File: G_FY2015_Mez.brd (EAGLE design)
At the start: 160 x 100 mm, 182 parts, among them IC100 FT232RL, J1 RPI2_GPIO_HOLES, J100 EPL.00.250.NTN, J101 EPL.00.250.NTN, J102 EPL.00.250.NTN, J103 EPL.00.250.NTN, J180 TOKUDEN_SP6, J181 USB Mini-B Connector, J2 SPACEWIRE_MDMMDM9, J300 SHV_PIGTAIL_LAND, J301 SHV_PIGTAIL_LAND, J600_12V IL-4P-S3EN2, J610 2.1MMJACKTHM, U10 LM60, U100 AD9215, U101 AD8138, U102 LM6142, U11 MCP4822-E/SN, U110 AD9215, U111 AD8138, U112 LM6142, U120 AD9215, U121 AD8138, U122 LM6142, U130 AD9215, U131 AD8138, U132 LM6142, U190 SN65LVDS049, U191 GPS_FGPMMOPA6H, U192 LED-5, U300 OPTON_1PA_12, U301 OPTON_1PA_12, U302 2SC1815, U303 2SJ313, U5 MCP3208-CI/SL, U500 LT6106, U510 LT6106, U6 MCP1525TSOT-23-3, U600 PHT12050WAH, U610 PHT12050WAH, U620 LTC1983ES6-3, U7 LM60, U8 LM60, U9 LM60

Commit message: version 20150904 (placement completed; before replacing with complementray SMD resistor and cap)
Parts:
- removed C192: 100n, Aardvark:3216
- removed C193: 4.7u, Aardvark:3216
- removed J102, J103: EPL.00.250.NTN, Aardvark:EPL.00.250.NTN
- removed JP1: (no value), pinhead:2X02
- removed JP100, TP_SPI: (no value), pinhead:1X05
- removed JP101: (no value), pinhead:1X06
- removed P_IN0, P_IN1, P_IN2, P_IN3, TP5: TPPAD1-13, Aardvark:P1-13
- removed R195, R196: 100, Aardvark:2012
- removed SJ1: (no value), Aardvark:SJ_2W
- removed U$27: (no value), Aardvark:AARDVARK_LOGO
- removed U$28: (no value), Aardvark:GROWTH_FY2015_LOGO
- removed U10, U9: LM60, Aardvark:TO-92-R2.5C
- removed U11: MCP4822-E/SN, Aardvark:SOIC-8(150MIL)(1.27MM)
- removed U190: SN65LVDS049, Aardvark:SO-16LD
- added C18: 1u, Aardvark:3216
- added C20, C22, C24, C26: 10u, Aardvark:3216
- added C21, C23, C25: 0.1u, Aardvark:3216
- added J110, J120, J130: EPL.00.250.NTN, Aardvark:EPL.00.250.NTN
- added J111, J121, J131, J620: IL-2P-S3EN2, Aardvark:IL-2P-S3EN2
- added J3: IL-3P-S3EN2, Aardvark:IL-3P-S3EN2
- added J4_I2C, J650_VOUT: IL-4P-S3EN2, Aardvark:IL-4P-S3EN2
- added J630, J640: USB_TYPEA_LUMBERG_2410_01, Aardvark:LUMBERG_2410-01
- added JP101_TRIG_OUT: (no value), Aardvark:2X07
- added JP_LCD: LCD16X2, Aardvark:LCD16X2
- added JP_SPI: (no value), Aardvark:1X05
- added R109, R119, R129, R139: 50, Aardvark:2012
- added R192: 2k, Aardvark:2012
- added R193: 1k, Aardvark:2012
- added SJ100, SJ110, SJ120, SJ130, SJ_ADC_MODE: (no value), Aardvark:SJ_2W
- added VR_CONT: (no value), Aardvark:ADJRP3-9.70XW5.0X9.80MM
- C19: value 100n -> 0.1u
- J101: value EPL.00.250.NTN -> IL-2P-S3EN2; device Aardvark:EPL.00.250.NTN -> Aardvark:IL-2P-S3EN2
- J2: value SPACEWIRE_MDMMDM9 -> IL-3P-S3EN2; device Aardvark:MDM_9_PCB -> Aardvark:IL-3P-S3EN2
- R190: value 1k -> 3k
- R500, R510: value 0.1 -> 0.01
- U100, U110, U120, U130: value AD9215 -> AD9215LONG_PAD; device Aardvark:TSSOP-28(4.4MM)(0.65MM) -> Aardvark:TSSOP-28(4.4MM)(0.65MM)_LONGPAD
- VR100, VR110, VR120, VR130: value 1k -> (none)
- moved U7 110.8 mm to (25.6, 27.9)
- moved TP_GND2 106.2 mm to (94.0, 2.17), turned to 90 degrees
- moved U510 71.7 mm to (91.9, 15.0)
- moved R510 70.5 mm to (91.2, 22.1), turned to 270 degrees
- moved R511 69.2 mm to (84.0, 19.7)
- moved R199 64.2 mm to (136.7, 24.6), flipped to the bottom, turned to 90 degrees
- moved R117 59.7 mm to (129.7, 42.8), turned to 0 degrees
- moved R115 57.6 mm to (134.7, 34.0), turned to 0 degrees
- moved R110 57.6 mm to (129.6, 37.9)
- moved R111 57.6 mm to (134.6, 37.9)
- moved R512 57.0 mm to (84.0, 24.7)
- moved R132 56.8 mm to (41.5, 9.35), flipped to the bottom, turned to 180 degrees
- moved P_OUT3 56.6 mm to (49.6, 26.1)
- moved TP_GND 56.5 mm to (5.70, 83.9)
- moved R137 55.9 mm to (45.4, 26.9), turned to 90 degrees
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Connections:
- removed net SLOWDAC_/LDAC: J1.P$3, U11.5
- removed net SLOWDAC_0: JP1.1, U11.8
- removed net SLOWDAC_1: JP1.3, U11.6
- removed net SPW_DIN_N: J2.6, R195.2, U190.1
- removed net SPW_DIN_P: J2.1, R195.1, U190.2
- removed net SPW_DOUT_N: J2.5, U190.8
- removed net SPW_DOUT_P: J2.9, U190.7
- removed net SPW_SIN_N: J2.7, R196.2, U190.4
- removed net SPW_SIN_P: J2.2, R196.1, U190.3
- removed net SPW_SOUT_N: J2.4, U190.5
- removed net SPW_SOUT_P: J2.8, U190.6
- removed net VREF_3V3_1/2: R190.2, R191.1, SJ1.1
- new net LCD_D4: J1.P$31, JP_LCD.11
- new net LCD_D5: J1.P$33, JP_LCD.12
- new net LCD_D6: J1.P$35, JP_LCD.13
- new net LCD_D7: J1.P$37, JP_LCD.14
- new net LCD_ENA: J1.P$40, JP_LCD.6
- new net LCD_RS: J1.P$38, JP_LCD.4
- new net LCD_V_CONT: JP_LCD.3, VR_CONT.2
- new net N$100: P_OUT0.TP, R109.2, U102.7, VR100.2
- new net N$101: R109.1, SJ100.1
- new net N$102: R119.1, SJ110.1
- new net N$103: R129.1, SJ120.1
- new net N$104: R139.1, SJ130.1
- new net N$34: J630.D-
- new net N$88: J630.D+
- new net N$89: J640.D-
- new net N$90: J640.D+
- new net N$91: JP101_TRIG_OUT.11
- new net N$92: P_OUT1.TP, R119.2, U112.7, VR110.2
- new net N$93: P_OUT2.TP, R129.2, U122.7, VR120.2
- new net N$94: JP_LCD.8
- new net N$95: JP_LCD.9
- new net N$96: JP_LCD.10
- new net N$97: JP_LCD.7
- new net N$98: P_OUT3.TP, R139.2, U132.7, VR130.2
- new net N$99: R192.2, R193.1, SJ_ADC_MODE.3
- new net RPI_I2C_SCL: J1.P$5, J4_I2C.P$2
- new net RPI_I2C_SDA: J1.P$3, J4_I2C.P$3
- net +3V3: now also C18.2, C20.2, C21.2, C22.2, C23.2, C24.2, C25.2, C26.2, J2.P$1, J3.P$1, J4_I2C.P$1, J650_VOUT.P$2, JP101_TRIG_OUT.14, R192.1; no longer C190.1, C191.1, C192.2, C193.2, IC100.20, IC100.4, U10.1, U11.1, U190.12, U190.16, U9.1
- net +5V: now also C190.1, C191.1, IC100.20, IC100.4, J620.P$1, J630.VBUS, J640.VBUS, J650_VOUT.P$1, JP101_TRIG_OUT.2, JP_LCD.1, VR_CONT.1; no longer J180.81
- net -3V3: now also J650_VOUT.P$3
- net ADC_CM: now also R190.2, R191.1; no longer SJ1.2
- net ADC_MODE: now also SJ_ADC_MODE.2; no longer J180.24
- net AGND: now also VR100.3, VR110.3, VR120.3, VR130.3; no longer VR100.1, VR110.1, VR120.1, VR130.1
- net FPGA_GPIO0: now also JP101_TRIG_OUT.9; no longer JP101.5
- net GND: now also C18.1, C20.1, C21.1, C22.1, C23.1, C24.1, C25.1, C26.1, J110.S1, J120.S1, J130.S1, J2.P$3, J3.P$3, J4_I2C.P$4, J620.P$2, J630.GND, J630.GND1, J630.GND2, J640.GND, J640.GND1, J640.GND2, J650_VOUT.P$4, JP101_TRIG_OUT.13, JP_LCD.2, JP_LCD.5, R193.2, SJ_ADC_MODE.1, VR300.3, VR301.3, VR_CONT.3; no longer C192.1, C193.1, J101.S1, J102.S1, J103.S1, J180.82, J2.3, J2.THREAD_1, J2.THREAD_2, JP1.2, JP1.4, JP101.6, U10.3, U11.7, U190.13, U190.9, U9.3, VR300.1, VR301.1
- net N$21: no longer JP100.1
- net N$22: no longer JP100.2
- net N$29: no longer JP100.3
- net N$30: no longer JP100.4
- net N$31: no longer JP100.5
- net N$35: no longer TP5.TP
- net N$5: now also VR300.1; no longer VR300.3
- net N$58: no longer P_IN0.TP
- net N$62: now also VR100.1; no longer VR100.2
- net N$7: now also VR301.1; no longer VR301.3
- net N$70: now also J110.1; no longer J101.1, P_IN1.TP
- net N$72: now also VR110.1; no longer VR110.2
- net N$75: now also J120.1; no longer J102.1, P_IN2.TP
- net N$77: now also VR120.1; no longer VR120.2
- net N$80: now also J130.1; no longer J103.1, P_IN3.TP
- net N$82: now also VR130.1; no longer VR130.2
- net PREAMP0_OUT: now also SJ100.2; no longer P_OUT0.TP, U102.7, VR100.3
- net PREAMP1_OUT: now also SJ110.2; no longer P_OUT1.TP, U112.7, VR110.3
- net PREAMP2_OUT: now also SJ120.2; no longer P_OUT2.TP, U122.7, VR120.3
- net PREAMP3_OUT: now also SJ130.2; no longer P_OUT3.TP, U132.7, VR130.3
- net SLOWADC_0: no longer SJ1.3
- net SLOWADC_2: now also J3.P$2; no longer U9.2
- net SLOWADC_3: now also J2.P$2; no longer U10.2
- net SPI_CE0: now also JP_SPI.4; no longer TP_SPI.4
- net SPI_CE1: now also JP_SPI.5; no longer TP_SPI.5, U11.2
- net SPI_MISO: now also JP_SPI.2; no longer TP_SPI.2
- net SPI_MOSI: now also JP_SPI.3; no longer TP_SPI.3, U11.4
- net SPI_SCLK: now also JP_SPI.1; no longer TP_SPI.1, U11.3
- net SPW_DIN: no longer U190.15
- net SPW_DOUT: no longer U190.10
- net SPW_SIN: no longer U190.14
- net SPW_SOUT: no longer U190.11
- net TRIG_OUT0: now also JP101_TRIG_OUT.1; no longer JP101.1
- net TRIG_OUT1: now also JP101_TRIG_OUT.3; no longer JP101.2
- net TRIG_OUT2: now also JP101_TRIG_OUT.5; no longer JP101.3
- net TRIG_OUT3: now also JP101_TRIG_OUT.7; no longer JP101.4
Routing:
- net GND: track 1382.9 -> 0.00 mm, vias 12 -> 0
- net +3V3: track 600.1 -> 0.00 mm, vias 19 -> 0
- net -3V3: track 285.5 -> 0.00 mm, vias 9 -> 0
- net +5V: track 217.6 -> 0.00 mm, vias 2 -> 0
- net ADC_CM: track 186.8 -> 0.00 mm, vias 2 -> 0
- net GPS_1PPS: track 133.0 -> 0.00 mm, vias 2 -> 0
- net SLOWADC_5: track 125.4 -> 0.00 mm, vias 5 -> 0
- net SLOWADC_4: track 121.8 -> 0.00 mm, vias 3 -> 0
- net ADC_PDWN: track 117.6 -> 0.00 mm, vias 4 -> 0
- net SLOWADC_0: track 116.4 -> 0.00 mm, vias 4 -> 0
- net HV_PWR_ENADIS: track 112.7 -> 0.00 mm, vias 2 -> 0
- net ADC_MODE: track 107.9 -> 0.00 mm, vias 3 -> 0
- net +12V: track 106.1 -> 0.00 mm, vias 1 -> 0
- net TRIG_OUT2: track 105.2 -> 0.00 mm
- net PREAMP0_OUT: track 103.9 -> 0.00 mm, vias 1 -> 0
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- removed copper zone on layer 1, net GND
- removed copper zone on layer 16, net GND
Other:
- board text added: "GROWTH-FY2015 Electronics Board Version 20150904"
- board text removed: "GROWTH-FW2015 Electronics Board Version 20150519"

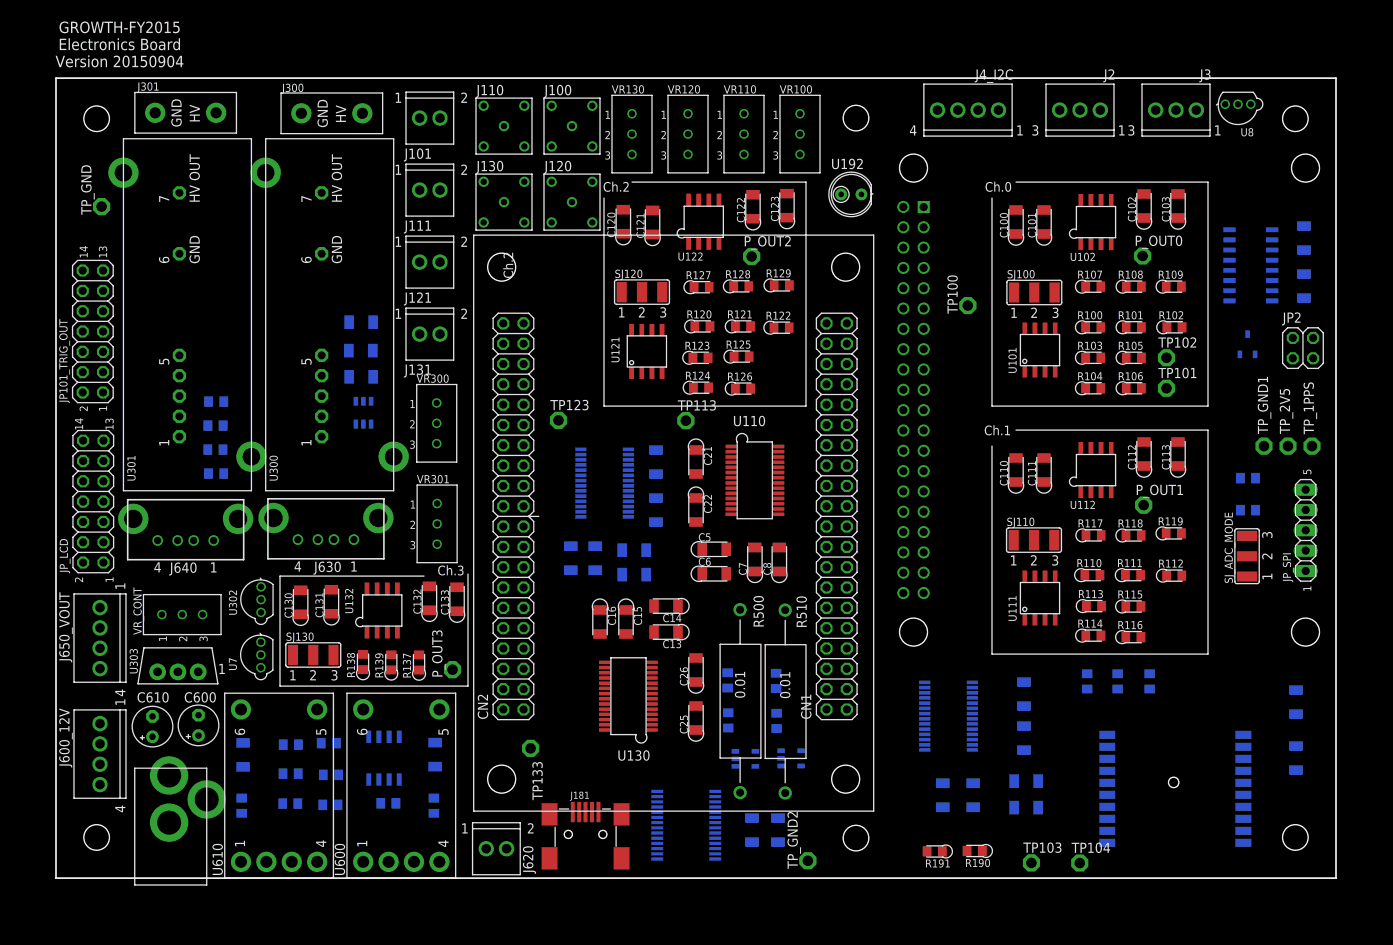
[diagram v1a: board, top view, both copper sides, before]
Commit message: as of 20150911 (4ch, FT232RL) before adding FT245 for higher data transfer rate
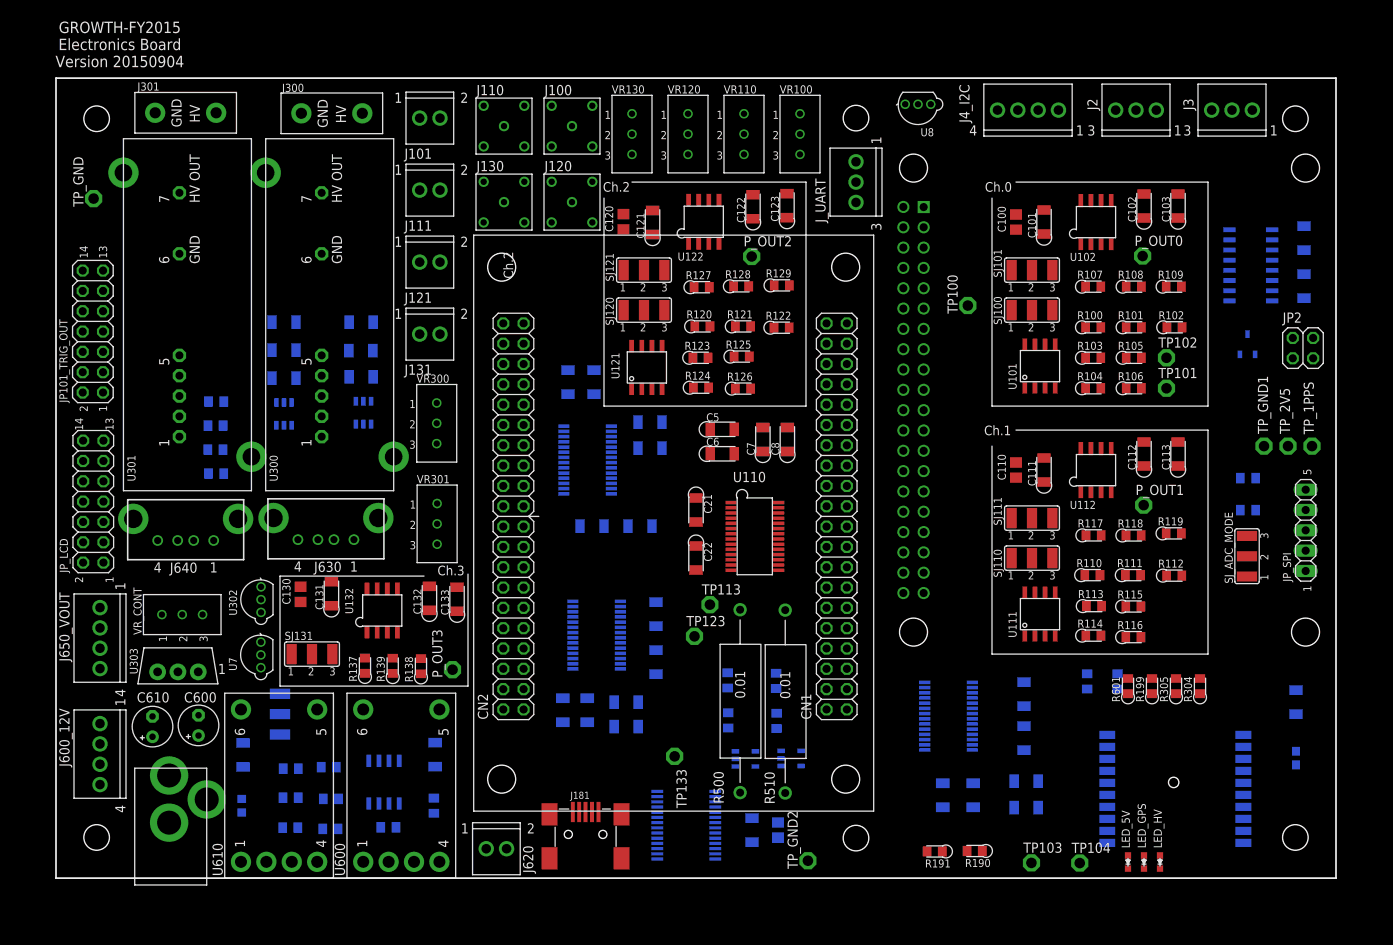
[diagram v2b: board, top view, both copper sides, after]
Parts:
- removed U192: LED-5, Aardvark:LED-5
- added C623, C624: 10u, Aardvark:3216
- added C625: 1u, Aardvark:3216
- added J_UART: IL-3P-S3EN2, Aardvark:IL-3P-S3EN2
- added LED_5V, LED_GPS, LED_HV: LED_1608, Aardvark:LED_1608
- added R304, R305: 1.2k, Aardvark:2012
- added R601: 82, Aardvark:2012
- added SJ101, SJ111, SJ121, SJ131: (no value), Aardvark:SJ_2W
- added U621: LTC1983ES6-5, Aardvark:SOT-23
- C100, C110, C120, C130, C191: device Aardvark:3216 -> Aardvark:C0805
- C190: value 100n -> 0.1u
- C194: device Aardvark:3216 -> Aardvark:C0603
- R100, R105, R106, R110, R115, R116, R120, R125, R126, R130, R135, R136: value 49.9 -> 51
- R101, R103, R104, R111, R113, R114, R121, R123, R124, R131, R133, R134: value 499 -> 510
- R102, R112, R122, R132: value 523 -> 510
- R109, R119, R129, R139: value 50 -> 51
- R199: value 330 -> 82
- R600: value 280 -> 270
- R610: device Aardvark:2012 -> Aardvark:R0603
- U102, U112, U122, U132: value LM6142 -> LM6172
- moved U8 40.0 mm to (107.8, 96.7)
- moved TP123 31.9 mm to (79.8, 30.2)
- moved C15 30.3 mm to (67.2, 62.0), flipped to the bottom
- moved C16 30.3 mm to (64.0, 62.0), flipped to the bottom
- moved U130 30.0 mm to (66.5, 52.3), flipped to the bottom, turned to 270 degrees
- moved C25 25.0 mm to (73.0, 44.0), flipped to the bottom, turned to 180 degrees
- moved TP113 23.2 mm to (81.7, 34.2)
- moved C13 23.1 mm to (74.2, 53.8), flipped to the bottom
- moved C14 23.1 mm to (74.2, 57.0), flipped to the bottom
- moved C26 22.2 mm to (67.0, 44.0), flipped to the bottom, turned to 180 degrees
- moved C9 19.0 mm to (71.3, 22.0)
- moved C10 19.0 mm to (71.3, 18.9)
- moved C11 19.0 mm to (66.4, 21.0)
- moved C12 19.0 mm to (63.4, 21.0)
- moved U120 19.0 mm to (67.6, 30.4)
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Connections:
- new net -5V: C103.2, C113.2, C123.2, C133.2, C624.1, U102.4, U112.4, U122.4, U132.4, U621.2
- new net AIN_0: J100.1, J101.P$1, SJ100.3, SJ101.1
- new net AIN_1: C110.1, R117.2, SJ110.3, SJ111.2, U112.2
- new net AIN_2: J120.1, J121.P$1, SJ120.3, SJ121.1
- new net AIN_3: J130.1, J131.P$1, SJ130.3, SJ131.1
- new net N$105: J110.1, J111.P$1, SJ111.1
- new net N$106: C100.1, R107.2, SJ101.2, U102.2
- new net N$108: C625.2, U621.3
- net +3V3: no longer C102.2, C112.2, C122.2, C132.2, U102.8, U112.8, U122.8, U132.8
- net +5V: now also C102.2, C112.2, C122.2, C132.2, C623.2, R601.2, U102.8, U112.8, U122.8, U132.8, U621.1, U621.6
- net -3V3: no longer C103.2, C113.2, C123.2, C133.2, U102.4, U112.4, U122.4, U132.4
- net GND: now also C623.1, C624.2, J101.P$2, J111.P$2, J121.P$2, J131.P$2, J_UART.P$3, LED_5V.P$2, LED_GPS.P$2, LED_HV.P$2, R101.1, R111.1, R121.1, R131.1, U621.5; no longer R102.2, R112.2, R122.2, R132.2, U192.2
- net HV_PWR_12V: now also R304.2, R305.2
- net N$58: now also LED_HV.P$1, R304.1, R305.1; no longer C100.1, J100.1, R107.2, U102.2
- net N$69: now also LED_GPS.P$1; no longer U192.1
- net N$70: now also LED_5V.P$1, R601.1; no longer C110.1, J110.1, R117.2, U112.2
- net N$75: now also C130.1, R137.2, SJ131.2, U132.2; no longer C120.1, J120.1, R127.2, U122.2
- net N$80: now also C120.1, R127.2, SJ121.2, U122.2; no longer C130.1, J130.1, R137.2, U132.2
- net N$91: now also C625.1, U621.4; no longer JP101_TRIG_OUT.11
- net PREAMP0_OUT: now also R102.2; no longer R101.1
- net PREAMP1_OUT: now also R112.2; no longer R111.1
- net PREAMP2_OUT: now also R122.2; no longer R121.1
- net PREAMP3_OUT: now also R132.2; no longer R131.1
- net RPI_RX_FPGA_TX: now also J_UART.P$1
- net RPI_TX_FPGA_RX: now also J_UART.P$2

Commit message: version B completed. before autoroute for P-ban submit
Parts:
- removed C1, C11, C12, C122, C123, C13, C132, C133, C15, C16, C19, C21, C23, C25, C3, C4, C5, C7, C8, C9: 0.1u, Aardvark:3216
- removed C10, C14, C2, C20, C22, C24, C26, C6: 10u, Aardvark:3216
- removed C120, C130: 100p, Aardvark:C0805
- removed C121, C131: ???, Aardvark:3216
- removed JP101_TRIG_OUT: (no value), Aardvark:2X07
- removed JP2: (no value), pinhead:2X02
- removed LED_GPS: LED_1608, Aardvark:LED_1608
- removed P_OUT2, P_OUT3, TP100, TP101, TP102, TP104, TP113, TP123, TP133: TPPAD1-13, Aardvark:P1-13
- removed R127, R137: 1M, Aardvark:2012
- removed R128, R138: ???, Aardvark:2012
- removed R129, R139: 51, Aardvark:2012
- removed R199: 82, Aardvark:2012
- removed R304, R305: 1.2k, Aardvark:2012
- removed SJ120, SJ121, SJ130, SJ131: (no value), Aardvark:SJ_2W
- removed U122, U132: LM6172, Aardvark:SOP8
- removed U7: LM60, Aardvark:TO-92-R2.5C
- removed VR120, VR130: (no value), Aardvark:ADJRP3-9.70XW5.0X9.80MM
- added -3V, -5V, AIN0+, AIN0-, AIN1+, AIN1-, GPIO0, GPIO1, VR100PIN2, VR110PIN2, VREF1, VREF2, VREF3, VR_HV0, VR_HV1: TPPAD1-13, Aardvark:P1-13
- added C104, C106, C107, C108, C114, C116, C117, C118, C124, C126, C127, C128, C134, C136, C137, C138, C192, C193: 0.1u, Aardvark:C0805
- added C105, C109, C115, C119, C125, C129, C135, C139: 10u, Aardvark:C0805
- added C197: 0.01u, Aardvark:C0603
- added C198: 10u, Aardvark:3216
- added IC101: FT245RL, Aardvark:SSOP28DB
- added J182: USB Mini-B Connector, Aardvark:MINIUSB5+4P-SMD-0.8-90D
- added JP_ADC: (no value), Aardvark:2X02
- added LED_5V_SW, LED_RPI: SML-311WTT86, Aardvark:LED_1608
- added R400: 680, Aardvark:2012
- added R520: 47k, Aardvark:2012
- added R521, R522: 4.7k, Aardvark:2012
- added R523: 1.5k, Aardvark:2012
- added R_PZC0, R_PZC1: 56k, Aardvark:2012
- added U412: LM60, Aardvark:TO-92-R2.5C
- added U520: 2SC1815, Aardvark:TO-92-R2.5C
- added U521: 2SJ681, Aardvark:2-7J2B
- C101, C111: value ??? -> 200p; device Aardvark:3216 -> Aardvark:C0805
- C102, C103, C112, C113: value 0.1u -> 0.033u; device Aardvark:3216 -> Aardvark:C0805
- C190: device Aardvark:3216 -> Aardvark:C0805
- C194: value 0.01u -> 4.7u; device Aardvark:C0603 -> Aardvark:C0805
- C195: value 10u -> 0.1u; device Aardvark:3216 -> Aardvark:C0805
- LED_5V, LED_HV: value LED_1608 -> SML-311WTT86
- R107, R117: value 1M -> 100k
- R108, R118: value ??? -> 10k
- R301: value 47k -> 4.7k
- R601: value 82 -> 1.5k
- R610: device Aardvark:R0603 -> Aardvark:2012
- U303: value 2SJ313 -> 2SJ681; device Aardvark:SC67-P -> Aardvark:2-7J2B
- VR100, VR110, VR_CONT: value (none) -> 5k
- moved LED_HV 129.6 mm to (11.5, 30.0), turned to 270 degrees
- moved LED_5V 125.2 mm to (11.5, 28.0), turned to 270 degrees
- moved R601 117.1 mm to (17.0, 28.0), flipped to the bottom, turned to 180 degrees
- moved R132 79.8 mm to (91.0, 69.0), flipped to the top, turned to 0 degrees
- moved R131 79.2 mm to (86.0, 69.0), flipped to the top
- moved R135 78.9 mm to (86.0, 65.0), flipped to the top
- moved R136 78.8 mm to (86.0, 61.0), flipped to the top
- moved C194 72.9 mm to (82.9, 26.0), flipped to the top
- moved R130 72.4 mm to (81.0, 69.0), flipped to the top
- moved R133 72.2 mm to (81.0, 65.0), flipped to the top
- moved R134 72.0 mm to (81.0, 61.0), flipped to the top
- moved C195 69.0 mm to (86.2, 25.9), flipped to the top
- moved TP_GND 68.1 mm to (71.8, 96.6), turned to 0 degrees
- moved U131 61.5 mm to (74.0, 63.9), flipped to the top
- moved R501 54.0 mm to (38.3, 35.1), turned to 0 degrees
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- renumbered C17 to C411, C18 to C410, J1 to J400, J2 to J411, J3 to J410, J4_I2C to J_I2C, TP103 to VREF0, TP_1PPS to 1PPS, TP_2V5 to 2.5V, TP_GND1 to GND, U5 to U410, U6 to U411, U8 to U413
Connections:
- removed net AGND: VR100.3, VR110.3, VR120.3, VR130.3
- removed net FT232_/CTS_FPGA_/RTS: IC100.11, J180.51
- removed net FT232_/RTS_FPGA_/CTS: IC100.3, J180.52
- removed net N$103: R129.1, SJ120.1
- removed net N$104: R139.1, SJ130.1
- removed net N$77: U122.6, VR120.1
- removed net N$78: C130.2, C131.1, R137.1, U132.1
- removed net N$79: C131.2, R138.1, U132.5
- removed net N$80: C120.1, R127.2, SJ121.2, U122.2
- removed net N$82: U132.6, VR130.1
- removed net N$86: R301.1, U302.2
- removed net N$93: P_OUT2.TP, R129.2, U122.7, VR120.2
- removed net N$98: P_OUT3.TP, R139.2, U132.7, VR130.2
- removed net PREAMP2_OUT: R120.2, R122.2, SJ120.2
- removed net PREAMP3_OUT: R130.2, R132.2, SJ130.2
- removed net RPI_RX_FPGA_TX: J180.25, J400.P$10, J_UART.P$1
- removed net RPI_TX_FPGA_RX: J180.29, J400.P$8, J_UART.P$2
- removed net SPW_DIN: J180.35
- removed net SPW_DOUT: J180.31
- removed net SPW_SIN: J180.37
- removed net SPW_SOUT: J180.33
- removed net TRIG_OUT0: J180.53, JP101_TRIG_OUT.1
- removed net TRIG_OUT1: J180.54, JP101_TRIG_OUT.3
- removed net TRIG_OUT2: J180.55, JP101_TRIG_OUT.5
- removed net TRIG_OUT3: J180.56, JP101_TRIG_OUT.7
- new net 5V_PWR_ENADIS: J400.P$32, R521.2
- new net 5V_SW_OUT: J630.VBUS, R523.2, U521.P$2
- new net FPGA_GPIO1: GPIO1.TP, J180.56
- new net FT245_/RE: IC101.13, J180.52
- new net FT245_/RXF: IC101.23, J180.24
- new net FT245_/TXE: IC101.22, J180.23
- new net FT245_D0: IC101.1, J180.25
- new net FT245_D1: IC101.5, J180.29
- new net FT245_D2: IC101.3, J180.31
- new net FT245_D3: IC101.11, J180.33
- new net FT245_D4: IC101.2, J180.35
- new net FT245_D5: IC101.9, J180.37
- new net FT245_D6: IC101.10, J180.53
- new net FT245_D7: IC101.6, J180.54
- new net FT245_WE: IC101.14, J180.51
- new net N$107: IC101.19
- new net N$109: IC101.27
- new net N$110: IC101.28
- new net N$111: IC101.17
- new net N$112: IC100.3
- new net N$113: IC100.11
- new net N$116: IC101.12
- new net RPI_LED0: J400.P$29, R400.2
- new net RPI_OUT_FPGA_IN0: J180.36, J400.P$7
- new net RPI_RX: J400.P$10, J_UART.P$1
- new net RPI_TX: J400.P$8, J_UART.P$2
- new net USB_D_M2: IC101.16, J182.2
- new net USB_D_P2: IC101.15, J182.3
- net +12V: now also U303.P$3; no longer U303.3
- net +3V3: now also C108.2, C109.2, C118.2, C119.2, C128.2, C129.2, C138.2, C139.2, C192.1, C195.1, C197.2, C198.2, IC100.4, IC101.4, U412.1; no longer C19.2, C194.2, C195.2, C20.2, C21.2, C22.2, C23.2, C24.2, C25.2, C26.2, JP101_TRIG_OUT.14, U7.1
- net +5V: now also C193.1, C194.1, IC101.20, R520.2, U521.P$3; no longer C122.2, C132.2, IC100.4, J630.VBUS, JP101_TRIG_OUT.2, U122.8, U132.8
- net -3V3: now also -3V.TP; no longer J650_VOUT.P$3
- net -5V: now also -5V.TP, J650_VOUT.P$3; no longer C123.2, C133.2, U122.4, U132.4
- net ADC0_CLK: no longer TP104.TP
- net ADC0_VIN_N: now also AIN0-.TP; no longer TP102.TP
- net ADC0_VIN_P: now also AIN0+.TP; no longer TP101.TP
- net ADC1_VIN_N: now also AIN1-.TP
- net ADC1_VIN_P: now also AIN1+.TP
- net ADC_PDWN: no longer J180.23
- net AIN_1: now also J110.1, J111.P$1, SJ111.1; no longer C110.1, R117.2, SJ111.2, U112.2
- net AIN_2: now also R120.2, R122.2; no longer SJ120.3, SJ121.1
- net AIN_3: now also R130.2, R132.2; no longer SJ130.3, SJ131.1
- net FPGA_GPIO0: now also GPIO0.TP, J180.55; no longer J180.36, JP101_TRIG_OUT.9
- net GND: now also C106.2, C107.2, C108.1, C109.1, C116.2, C117.2, C118.1, C119.1, C126.2, C127.2, C128.1, C129.1, C136.2, C137.2, C138.1, C139.1, C192.2, C193.2, C194.2, C195.2, C197.1, C198.1, IC101.18, IC101.21, IC101.25, IC101.26, IC101.7, J182.5, J182.P$1, J182.P$2, J182.P$3, J182.P$4, JP_ADC.2, JP_ADC.4, LED_5V_SW.P$2, LED_RPI.P$2, R302.2, R522.2, U412.3, U520.1, VR100.1, VR110.1, VR300.1, VR301.1; no longer C11.2, C12.2, C122.1, C123.1, C132.1, C133.1, C15.2, C16.2, C19.1, C194.1, C195.1, C20.1, C21.1, C22.1, C23.1, C24.1, C25.1, C26.1, C3.2, C4.2, C7.2, C8.2, JP101_TRIG_OUT.13, JP2.2, JP2.4, LED_GPS.P$2, R128.2, R138.2, R303.2, U122.3, U132.3, U7.3, VR300.3, VR301.3
- net HV_PWR_12V: now also R303.2, U303.P$2; no longer R304.2, R305.2, U303.2
- net HV_PWR_ENADIS: now also R301.2; no longer R302.2
- net N$100: now also VR100.3; no longer P_OUT0.TP, VR100.2
- net N$105: now also C110.1, R117.2, SJ111.2, U112.2; no longer J110.1, J111.P$1, SJ111.1
- net N$11: now also C104.2, C105.2, C106.1; no longer C1.2, C2.2, C3.1
- net N$12: now also VREF1.TP; no longer TP113.TP
- net N$13: now also C114.2, C115.2, C116.1; no longer C5.2, C6.2, C7.1
- net N$14: now also C104.1, C105.1, C107.1; no longer C1.1, C2.1, C4.1
- net N$15: now also C114.1, C115.1, C117.1; no longer C5.1, C6.1, C8.1
- net N$16: now also VREF2.TP; no longer TP123.TP
- net N$17: now also C124.2, C125.2, C126.1; no longer C10.2, C11.1, C9.2
- net N$18: now also C124.1, C125.1, C127.1; no longer C10.1, C12.1, C9.1
- net N$19: now also VREF3.TP; no longer TP133.TP
- net N$20: now also C134.2, C135.2, C136.1; no longer C13.2, C14.2, C15.1
- net N$23: now also C134.1, C135.1, C137.1; no longer C13.1, C14.1, C16.1
- net N$3: now also VR_HV0.TP
- net N$5: now also VR300.3; no longer VR300.1
- net N$54: now also R_PZC0.1
- net N$55: now also R_PZC0.2
- net N$58: now also R303.1; no longer R304.1, R305.1
- net N$6: now also VR_HV1.TP
- net N$61: now also R_PZC1.1
- net N$62: now also U112.6, VR110.2, VR110PIN2.TP; no longer U102.6, VR100.1
- net N$63: now also R_PZC1.2
- net N$65: no longer R199.2
- net N$69: now also LED_RPI.P$1, R400.1; no longer LED_GPS.P$1, R199.1
- net N$7: now also VR301.3; no longer VR301.1
- net N$72: now also R520.1, U520.2, U521.P$1; no longer U112.6, VR110.1
- net N$73: now also U102.6, VR100.2, VR100PIN2.TP; no longer C120.2, C121.1, R127.1, U122.1
- net N$74: now also R521.1, R522.1, U520.3; no longer C121.2, R128.1, U122.5
- net N$75: now also LED_5V_SW.P$1, R523.1; no longer C130.1, R137.2, SJ131.2, U132.2
- net N$85: now also U302.2, U303.P$1; no longer R301.2, U303.1
- net N$87: now also R301.1; no longer R303.1
- net N$92: now also VR110.3; no longer P_OUT1.TP, VR110.2
- net PREAMP0_OUT: now also P_OUT0.TP; no longer TP100.TP
- net PREAMP1_OUT: now also P_OUT1.TP
- net SLOWADC_0: now also U412.2; no longer U7.2
- net SLOWADC_6: now also JP_ADC.1; no longer JP2.1
- net SLOWADC_7: now also JP_ADC.3; no longer JP2.3
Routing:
- added copper zone on layer 1, net GND
- added copper zone on layer 16, net GND
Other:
- board text added: "AIN6"
- board text added: "AIN7"
- board text added: "GND"
- board text added: "GROWTH-FY2015 Electronics Board Version B"
- board text removed: "Ch.3"
- board text removed: "GROWTH-FY2015 Electronics Board Version 20150904"
